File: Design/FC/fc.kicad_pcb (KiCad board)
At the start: 4 copper layers, 70.8 x 100 mm, 115 parts, among them J1 XT60PW-M, U1 STM32H747BIT6, U2 INA219AIDCNT

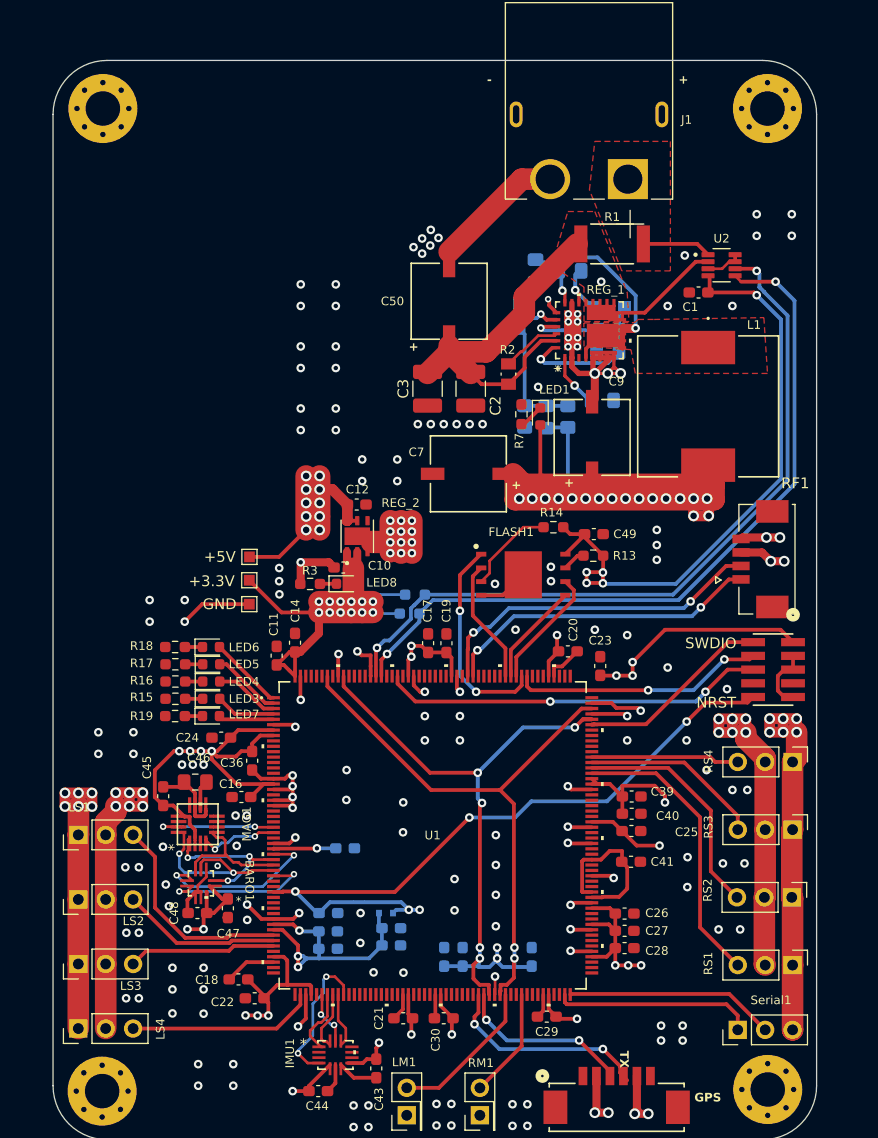
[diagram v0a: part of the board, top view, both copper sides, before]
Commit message: updated silkscreen
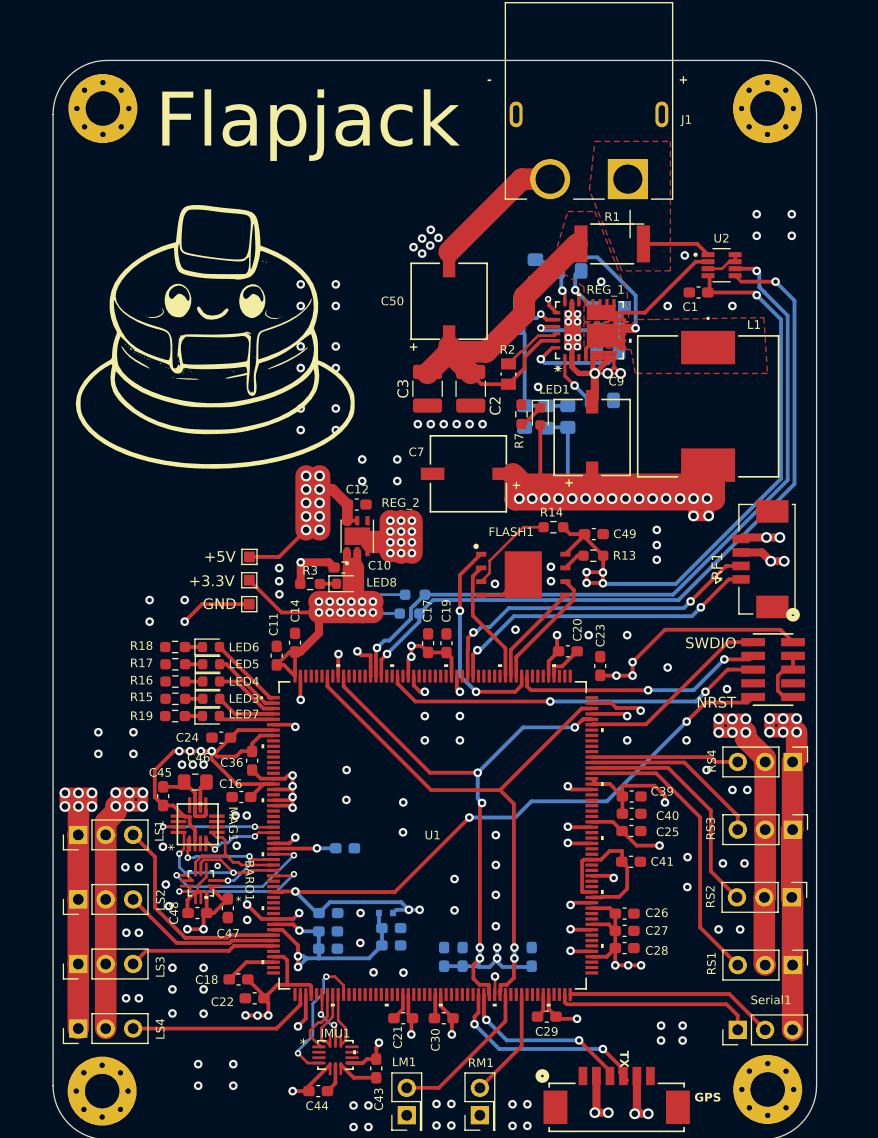
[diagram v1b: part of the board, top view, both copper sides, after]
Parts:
- added G***: LOGO, Silkscreen:Flapjack_Icon, F.Cu at (178.0, 76.5)
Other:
- board text added: "Flapjack"

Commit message: silkscreen
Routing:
- net GND: vias 195 -> 202
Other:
- board text added: "+5V"
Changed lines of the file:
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@@
 			(disableapertmacros no)
 			(usegerberextensions no)
-			(usegerberattributes yes)
-			(usegerberadvancedattributes yes)
-			(creategerberjobfile yes)
+			(usegerberattributes no)
+			(usegerberadvancedattributes no)
+			(creategerberjobfile no)
 			(dashed_line_dash_ratio 12.000000)
 			(dashed_line_gap_ratio 3.000000)
@@
 			(sketchdnponfab yes)
 			(crossoutdnponfab yes)
-			(subtractmaskfromsilk no)
+			(subtractmaskfromsilk yes)
 			(outputformat 1)
 			(mirror no)
-			(drillshape 1)
+			(drillshape 0)
 			(scaleselection 1)
-			(outputdirectory "")
+			(outputdirectory "Build/")
 		)
 	)
@@
 		(tags "BMP390 ")
 		(property "Reference" "BARO1"
-			(at -4.499999 0.25 270)
+			(at -3.849999 0.25 270)
 			(unlocked yes)
 			(layer "F.SilkS")
 			(effects
 				(font
-					(size 0.8 0.8)
-					(thickness 0.15)
+					(size 0.5 0.5)
+					(thickness 0.0625)
 				)
 			)
@@
 		(tags "MMC5983MA ")
 		(property "Reference" "MAG1"
-			(at 0.029407 3.272042 270)
+			(at -0.56889 3.127814 270)
 			(unlocked yes)
 			(layer "F.SilkS")
 			(effects
 				(font
-					(size 0.8 0.8)
-					(thickness 0.15)
+					(size 0.5 0.5)
+					(thickness 0.0625)
 				)
 			)
@@
 		(at 229.19914 97.212861 90)
 		(property "Reference" "RF1"
-			(at -0.662783 -4.60175 270)
+			(at 1.412861 -4.79914 270)
 			(layer "F.SilkS")
 			(effects
@@
 		)
 		(fp_text user "*"
-			(at -3.5398 -2.6 90)
-			(layer "F.SilkS")
-			(effects
-				(font
-					(size 1 1)
-					(thickness 0.15)
-				)
-			)
-		)
-		(fp_text user "*"
 			(at -3.5398 -2.75 90)
 			(layer "F.SilkS")
@@
 		(tags "CFP3 SOD-123W")
 		(property "Reference" "D1"
-			(at 0.545258 -1.896909 180)
+			(at 3.4 0.103091 180)
 			(layer "B.SilkS")
 			(effects
@@
 		(tags "resistor handsolder")
 		(property "Reference" "R10"
-			(at 2.4125 1.5 0)
+			(at 2.9125 0.15 0)
 			(layer "B.SilkS")
 			(effects
@@
 		(tags "capacitor handsolder")
 		(property "Reference" "C5"
-			(at 0 1.68 90)
+			(at -2.9 -0.05 90)
 			(layer "B.SilkS")
 			(effects
@@
 		(tags "resistor handsolder")
 		(property "Reference" "R9"
-			(at -0.0875 -1.25 180)
+			(at 2.6125 0.1 180)
 			(layer "B.SilkS")
 			(effects
@@
 		(tags "capacitor handsolder")
 		(property "Reference" "C51"
-			(at 0 1.68 0)
+			(at -3.342356 0.006134 0)
 			(layer "B.SilkS")
 			(effects
@@
 		(at 206.25 74.675 90)
 		(property "Reference" "R4"
-			(at 0 -1.5 90)
+			(at 2.875 -0.25 90)
 			(layer "B.SilkS")
 			(effects
@@
 		(tags "capacitor handsolder")
 		(property "Reference" "C4"
-			(at 0 1.68 180)
+			(at 3.052799 0.1 180)
 			(layer "B.SilkS")
 			(effects
@@
 		(tags "resistor handsolder")
 		(property "Reference" "R5"
-			(at 2.5 0 0)
+			(at 2.8 -0.05 90)
 			(layer "B.SilkS")
 			(effects
@@
 		(tags "capacitor handsolder")
 		(property "Reference" "C8"
-			(at 2.7875 0 90)
+			(at -2.703405 -0.057549 270)
 			(layer "B.SilkS")
 			(effects
@@
 		(tags "resistor handsolder")
 		(property "Reference" "R6"
-			(at -2.5 0 180)
+			(at -2.708075 0.044872 270)
 			(layer "B.SilkS")
 			(effects
@@
 		(tags "capacitor handsolder")
 		(property "Reference" "C6"
-			(at 0 1.68 0)
+			(at -3.052799 0.1 0)
 			(layer "B.SilkS")
 			(effects
@@
 		)
 	)
+	(gr_text "+5V"
+		(at 216.6 141.2 270)
+		(layer "F.SilkS")
+		(effects
+			(font
+				(size 0.8 0.8)
+				(thickness 0.15)
+				(bold yes)
+			)
+			(justify left bottom)
+		)
+	)
 	(gr_text "GPS"
 		(at 222.471509 147.558988 0)
@@
 	)
 	(gr_text "TX"
-		(at 215.5 142.75 -90)
+		(at 215.4 142.2 -90)
 		(layer "F.SilkS")
 		(effects
@@
 	)
 	(gr_text "+"
-		(at 205.523045 90.811723 0)
+		(at 205.4 91 0)
 		(layer "F.SilkS")
 		(effects
@@
 		)
 	)
-	(gr_text "TX RX GND"
-		(at 228.25 138.381503 270)
-		(layer "B.SilkS")
+	(gr_text "TX"
+		(at 224.4 99.2 0)
+		(layer "F.SilkS")
 		(effects
 			(font
-				(size 0.8 0.8)
+				(size 1 1)
 				(thickness 0.15)
-				(bold yes)
 			)
-			(justify left bottom mirror)
 		)
 	)
-	(gr_text "GND PWM"
-		(at 195.75 150.25 270)
+	(gr_text "TX RX GND"
+		(at 228.25 138.381503 270)
 		(layer "B.SilkS")
 		(effects
@@
 		)
 	)
-	(gr_text "+"
-		(at 191.507225 131.832356 0)
+	(gr_text "GND PWM"
+		(at 195.75 150.25 270)
 		(layer "B.SilkS")
 		(effects
@@
 				(bold yes)
 			)
-			(justify left bottom)
+			(justify left bottom mirror)
 		)
 	)
@@
 		)
 	)
-	(gr_text "TX"
-		(at 226.75 99.25 -0)
-		(layer "B.SilkS")
-		(effects
-			(font
-				(size 1 1)
-				(thickness 0.15)
-			)
-			(justify mirror)
-		)
-	)
 	(gr_text "GND +5V PWM"
 		(at 163.75 127 180)
@@
 	)
 	(via
-		(at 221.84238 124.82285)
+		(at 221.6 131.614981)
+		(size 0.8)
+		(drill 0.4)
+		(layers "F.Cu" "B.Cu")
+		(net 160)
+	)
+	(via
+		(at 221.6 121.414981)
 		(size 0.8)
 		(drill 0.4)
@@
 	)
 	(via
+		(at 221.6 133)
+		(size 0.8)
+		(drill 0.4)
+		(layers "F.Cu" "B.Cu")
+		(net 160)
+	)
+	(via
 		(at 204 99.5)
 		(size 0.8)
@@
 	)
 	(via
+		(at 221.6 122.8)
+		(size 0.8)
+		(drill 0.4)
+		(layers "F.Cu" "B.Cu")
+		(net 160)
+	)
+	(via
 		(at 191.544459 130)
 		(size 0.8)
@@
 	)
 	(via
+		(at 218.229962 127.6)
+		(size 0.8)
+		(drill 0.4)
+		(layers "F.Cu" "B.Cu")
+		(net 160)
+	)
+	(via
 		(at 213.25 148.5)
 		(size 1)
@@
 	)
 	(via
+		(at 219.614981 127.6)
+		(size 0.8)
+		(drill 0.4)
+		(layers "F.Cu" "B.Cu")
+		(net 160)
+	)
+	(via
 		(at 199.957442 149.688347)
 		(size 0.8)
@@
 	)
 	(via
+		(at 221 127.6)
+		(size 0.8)
+		(drill 0.4)
+		(layers "F.Cu" "B.Cu")
+		(net 160)
+	)
+	(via
 		(at 226 73.75)
 		(size 0.8)
@@
 	)
 	(via
-		(at 221.82022 127.592888)
+		(at 221.6 124.185019)
 		(size 0.8)
 		(drill 0.4)
@@
 		(size 0.8)
 		(drill 0.4)
+		(layers "F.Cu" "B.Cu")
+		(net 160)
+	)
+	(via
+		(at 221.6 130.229962)
+		(size 0.8)
+		(drill 0.4)
